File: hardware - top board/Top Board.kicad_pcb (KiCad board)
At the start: 2 copper layers, 60 x 60 mm, 4 parts

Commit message: PCB artwork + output
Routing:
- added copper zone on B.Cu, net (none)
- added copper zone on F.Cu, net (none)
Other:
- board text added: "(C)2024 Kuro68k"

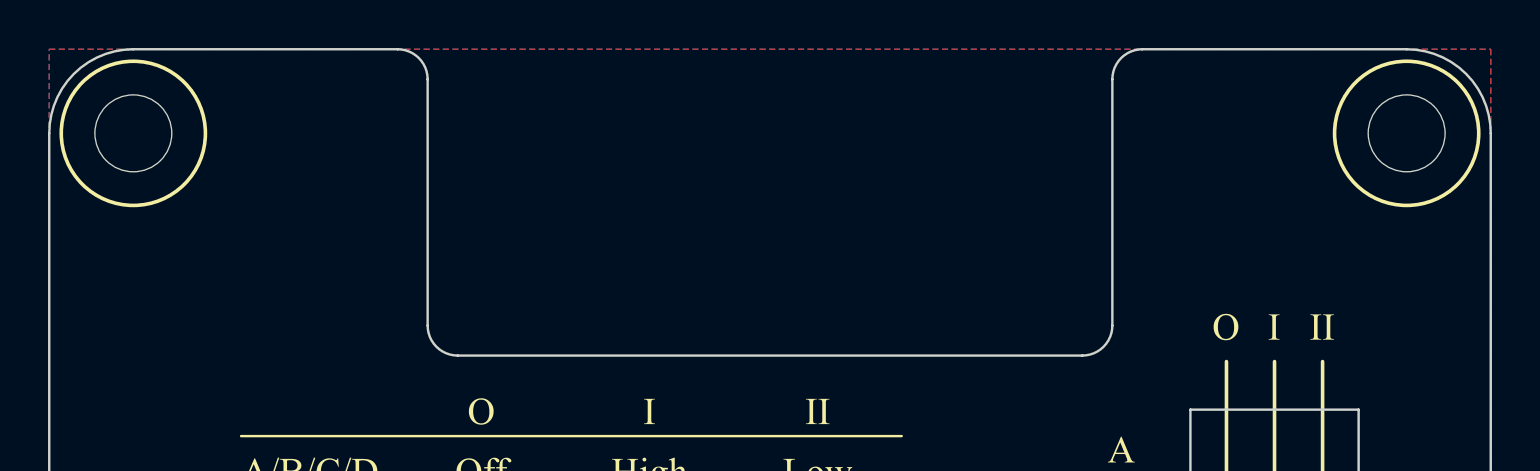
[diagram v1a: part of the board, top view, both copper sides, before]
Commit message: Playstation 3V3 power and signalling
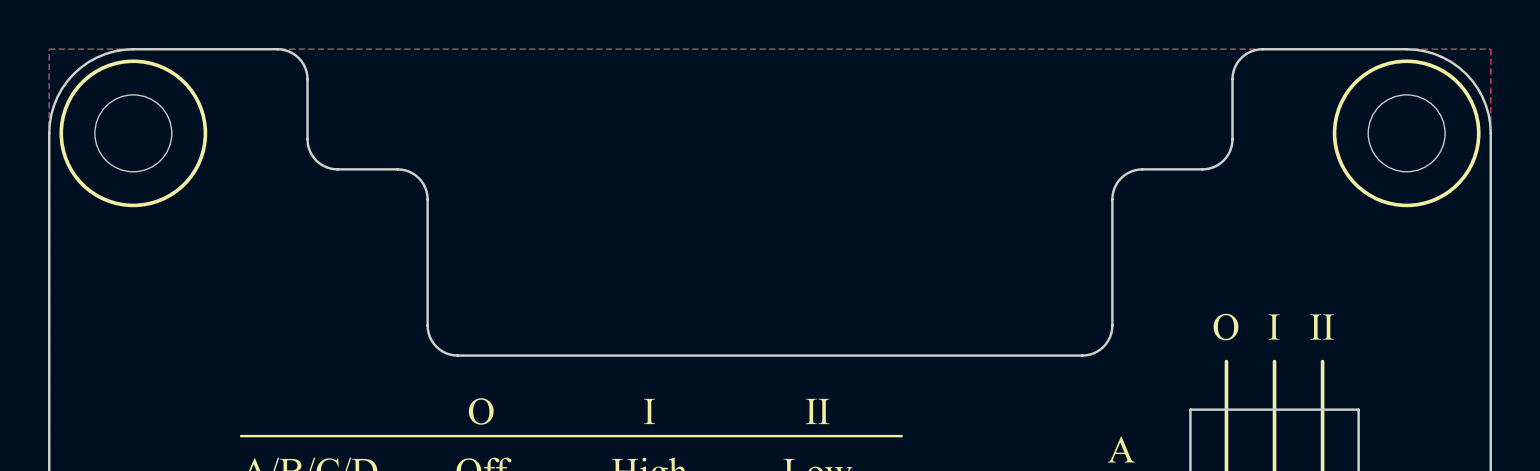
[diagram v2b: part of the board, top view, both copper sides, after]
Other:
- outline, holes or cut-outs redrawn
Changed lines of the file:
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@@
+	)
+	(gr_line
+		(start 124.25 41.25)
+		(end 124.25 43.75)
+		(stroke
+			(width 0.1)
+			(type default)
+		)
+		(layer "Edge.Cuts")
 	)
 	(gr_line
 		(start 131.5 40)
-		(end 120.5 40)
+		(end 125.5 40)
+		(stroke
+			(width 0.1)
+			(type default)
+		)
+		(layer "Edge.Cuts")
+	)
+	(gr_line
+		(start 123 45)
+		(end 120.5 45)
 		(stroke
 			(width 0.1)
@@
 		(layer "Edge.Cuts")
 	)
-	(gr_arc
-		(start 119.25 41.25)
-		(mid 119.616117 40.366117)
-		(end 120.5 40)
+	(gr_line
+		(start 87 45)
+		(end 89.5 45)
+		(stroke
+			(width 0.1)
+			(type default)
+		)
+		(layer "Edge.Cuts")
+	)
+	(gr_arc
+		(start 119.25 46.25)
+		(mid 119.616117 45.366117)
+		(end 120.5 45)
 		(stroke
 			(width 0.1)
@@
 	(gr_line
 		(start 90.75 51.5)
-		(end 90.75 41.25)
+		(end 90.75 46.25)
 		(stroke
 			(width 0.1)
@@
 		(layer "Edge.Cuts")
 	)
+	(gr_arc
+		(start 84.5 40)
+		(mid 85.383883 40.366117)
+		(end 85.75 41.25)
+		(stroke
+			(width 0.1)
+			(type default)
+		)
+		(layer "Edge.Cuts")
+	)
 	(gr_line
 		(start 131.5 100)
@@
 	)
 	(gr_arc
-		(start 89.5 40)
-		(mid 90.383883 40.366117)
-		(end 90.75 41.25)
+		(start 124.25 41.25)
+		(mid 124.616117 40.366117)
+		(end 125.5 40)
+		(stroke
+			(width 0.1)
+			(type default)
+		)
+		(layer "Edge.Cuts")
+	)
+	(gr_arc
+		(start 89.5 45)
+		(mid 90.383883 45.366117)
+		(end 90.75 46.25)
+		(stroke
+			(width 0.1)
+			(type default)
+		)
+		(layer "Edge.Cuts")
+	)
+	(gr_arc
+		(start 87 45)
+		(mid 86.116117 44.633883)
+		(end 85.75 43.75)
+		(stroke
+			(width 0.1)
+			(type default)
+		)
+		(layer "Edge.Cuts")
+	)
+	(gr_arc
+		(start 124.25 43.75)
+		(mid 123.883883 44.633883)
+		(end 123 45)
 		(stroke
 			(width 0.1)
@@
 	)
 	(gr_line
+		(start 85.75 41.25)
+		(end 85.75 43.75)
+		(stroke
+			(width 0.1)
+			(type default)
+		)
+		(layer "Edge.Cuts")
+	)
+	(gr_line
 		(start 119.25 51.5)
-		(end 119.25 41.25)
+		(end 119.25 46.25)
 		(stroke
 			(width 0.1)
@@
 	)
 	(gr_line
-		(start 89.5 40)
+		(start 84.5 40)
 		(end 78.5 40)
 		(stroke

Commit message: Rev 2 RTM
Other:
- outline, holes or cut-outs redrawn
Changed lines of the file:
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@@
 	)
 	(paper "A4")
+	(title_block
+		(rev "2")
+	)
 	(layers
 		(0 "F.Cu" signal)
@@
 			(drillshape 0)
 			(scaleselection 1)
-			(outputdirectory "")
+			(outputdirectory "plot/")
 		)
 	)
@@
 				(font
 					(size 1.27 1.27)
+					(thickness 0.15)
 				)
 			)
@@
 				(font
 					(size 1.27 1.27)
+					(thickness 0.15)
 				)
 			)
@@
 				(font
 					(size 1.27 1.27)
+					(thickness 0.15)
 				)
 			)
@@
 				(font
 					(size 1.27 1.27)
+					(thickness 0.15)
 				)
 			)
@@
 				(font
 					(size 1.27 1.27)
+					(thickness 0.15)
 				)
 			)
@@
 				(font
 					(size 1.27 1.27)
+					(thickness 0.15)
 				)
 			)
@@
 				(font
 					(size 1.27 1.27)
+					(thickness 0.15)
 				)
 			)
@@
 				(font
 					(size 1.27 1.27)
+					(thickness 0.15)
 				)
 			)
@@
 				(font
 					(size 1.27 1.27)
+					(thickness 0.15)
 				)
 			)
@@
 				(font
 					(size 1.27 1.27)
+					(thickness 0.15)
 				)
 			)
@@
 				(font
 					(size 1.27 1.27)
+					(thickness 0.15)
 				)
 			)
@@
 				(font
 					(size 1.27 1.27)
+					(thickness 0.15)
 				)
 			)
@@
 		(layer "F.SilkS")
 	)
-	(gr_circle
-		(center 78.5 96.5)
-		(end 81.5 96.5)
-		(stroke
-			(width 0.15)
-			(type default)
-		)
-		(fill none)
-		(layer "F.SilkS")
-	)
 	(gr_poly
 		(pts
@@
 		(layer "F.SilkS")
 	)
-	(gr_circle
-		(center 131.5 43.5)
-		(end 134.5 43.5)
-		(stroke
-			(width 0.15)
-			(type default)
-		)
-		(fill none)
-		(layer "F.SilkS")
-	)
 	(gr_poly
 		(pts
@@
 		(layer "F.SilkS")
 	)
-	(gr_circle
-		(center 131.5 96.5)
-		(end 134.5 96.5)
-		(stroke
-			(width 0.15)
-			(type default)
-		)
-		(fill none)
-		(layer "F.SilkS")
-	)
 	(gr_poly
 		(pts
@@
 		(layer "F.SilkS")
 	)
-	(gr_circle
-		(center 78.5 43.5)
-		(end 75.5 43.5)
-		(stroke
-			(width 0.15)
-			(type default)
-		)
-		(fill none)
-		(layer "F.SilkS")
-	)
 	(gr_poly
 		(pts
@@
 	)
 	(gr_line
-		(start 124.25 41.25)
-		(end 124.25 43.75)
+		(start 126.25 41.25)
+		(end 126.25 43.75)
 		(stroke
 			(width 0.1)
@@
 	(gr_line
 		(start 131.5 40)
-		(end 125.5 40)
+		(end 127.5 40)
 		(stroke
 			(width 0.1)
@@
 	)
 	(gr_line
-		(start 123 45)
+		(start 125 45)
 		(end 120.5 45)
 		(stroke
@@
 	)
 	(gr_line
-		(start 87 45)
+		(start 85 45)
 		(end 89.5 45)
 		(stroke
@@
 	)
 	(gr_arc
-		(start 84.5 40)
-		(mid 85.383883 40.366117)
-		(end 85.75 41.25)
+		(start 82.5 40)
+		(mid 83.383883 40.366117)
+		(end 83.75 41.25)
 		(stroke
 			(width 0.1)
@@
 	)
 	(gr_arc
-		(start 124.25 41.25)
-		(mid 124.616117 40.366117)
-		(end 125.5 40)
+		(start 126.25 41.25)
+		(mid 126.616117 40.366117)
+		(end 127.5 40)
 		(stroke
 			(width 0.1)
@@
 	)
 	(gr_arc
-		(start 87 45)
-		(mid 86.116117 44.633883)
-		(end 85.75 43.75)
+		(start 85 45)
+		(mid 84.116117 44.633883)
+		(end 83.75 43.75)
 		(stroke
 			(width 0.1)
@@
 	)
 	(gr_arc
-		(start 124.25 43.75)
-		(mid 123.883883 44.633883)
-		(end 123 45)
+		(start 126.25 43.75)
+		(mid 125.883883 44.633883)
+		(end 125 45)
 		(stroke
 			(width 0.1)
@@
 	)
 	(gr_line
-		(start 85.75 41.25)
-		(end 85.75 43.75)
+		(start 83.75 41.25)
+		(end 83.75 43.75)
 		(stroke
 			(width 0.1)
@@
 	)
 	(gr_line
-		(start 84.5 40)
+		(start 82.5 40)
 		(end 78.5 40)
 		(stroke
